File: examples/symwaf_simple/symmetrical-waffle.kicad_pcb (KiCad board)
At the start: 2 copper layers, 38 parts, among them J1 ICSP, J2 FTDI Programmer, J3 GPIO Header, SW1 SW_Push, SW2 SW_DIP_x01, U1 ATMEGA328-AU, U10 ws2812b, U11 ws2812b, U12 ws2812b, U13 ws2812b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

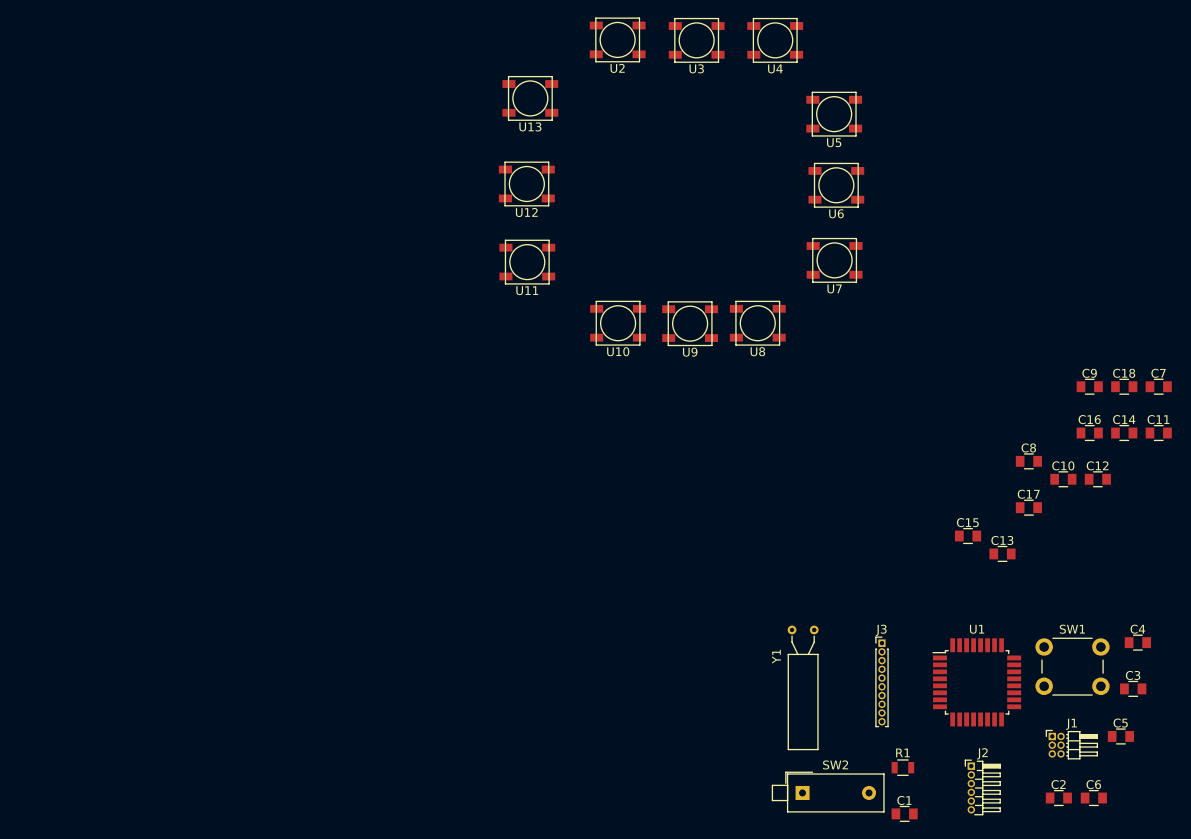
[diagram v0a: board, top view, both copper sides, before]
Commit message: Creating a simpler version of the example board
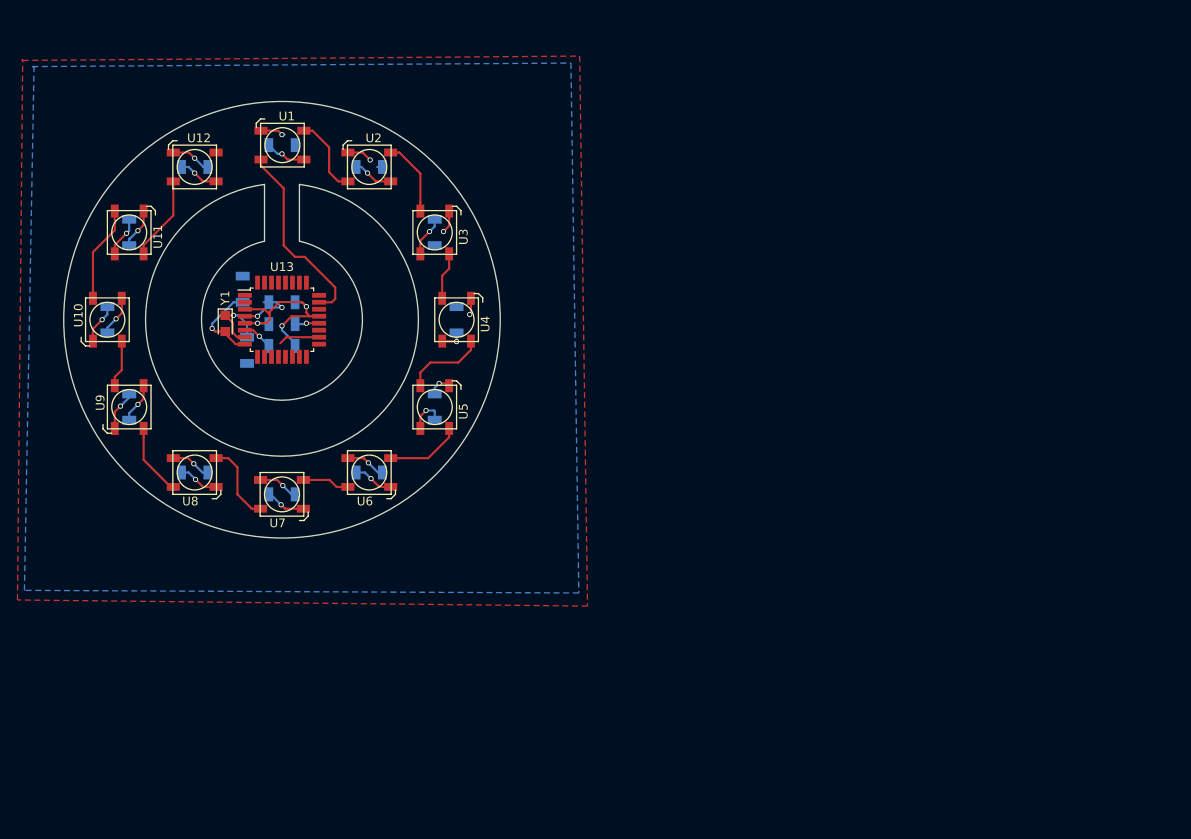
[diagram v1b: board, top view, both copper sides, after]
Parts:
- removed C18: C, Capacitors_SMD:C_0805
- removed J1: ICSP, Pin_Headers:Pin_Header_Angled_2x03_Pitch1.00mm
- removed J2: FTDI Programmer, Pin_Headers:Pin_Header_Angled_1x06_Pitch1.00mm
- removed J3: GPIO Header, Pin_Headers:Pin_Header_Straight_1x10_Pitch1.00mm
- removed R1: 10K, Resistors_SMD:R_0805
- removed SW1: SW_Push, Buttons_Switches_THT:SW_PUSH_6mm_h5mm
- removed SW2: SW_DIP_x01, Buttons_Switches_THT:SW_DIP_x1_W7.62mm_Piano
- C1, C2, C3: value 1nF -> C; footprint Capacitors_SMD:C_0805 -> Capacitors_SMD:C_1206; moved to B.Cu
- C10, C11, C12, C7, C8, C9: footprint Capacitors_SMD:C_0805 -> Capacitors_SMD:C_1206; moved to B.Cu
- C13, C14, C15: value C -> 1nF; footprint Capacitors_SMD:C_0805 -> Capacitors_SMD:C_1206; moved to B.Cu
- C16, C17: value C -> 22pF; footprint Capacitors_SMD:C_0805 -> Capacitors_SMD:C_1206; moved to B.Cu
- C4: value 100nF -> C; footprint Capacitors_SMD:C_0805 -> Capacitors_SMD:C_1206; moved to B.Cu
- C5, C6: value 22pF -> C; footprint Capacitors_SMD:C_0805 -> Capacitors_SMD:C_1206; moved to B.Cu
- U1: value ATMEGA328-AU -> ws2812b; footprint Housings_QFP:TQFP-32_7x7mm_Pitch0.8mm -> symwaf:ws2812b
- U13: value ws2812b -> ATMEGA328-AU; footprint symwaf:ws2812b -> Housings_QFP:TQFP-32_7x7mm_Pitch0.8mm
- Y1: footprint Crystals:Crystal_AT310_d3.0mm_l10.0mm_Horizontal -> Crystals:Crystal_SMD_2012-2pin_2.0x1.2mm_HandSoldering
- moved C11 120.1 mm to (70.0, 85.0), turned to 270 degrees
- moved C10 111.0 mm to (67.5, 95.0), turned to 90 degrees
- moved C9 110.0 mm to (70.0, 105.0), turned to 90 degrees
- moved C12 109.5 mm to (77.5, 77.5)
- moved C2 107.1 mm to (97.5, 77.5)
- moved C1 104.7 mm to (87.5, 75.0)
- moved C7 101.2 mm to (87.5, 115.0), turned to 180 degrees
- moved U1 100.6 mm to (87.5, 75.0), turned to 180 degrees
- moved C14 97.0 mm to (87.5, 98.0)
- moved C16 97.0 mm to (83.5, 98.5), turned to 90 degrees
- moved C3 95.6 mm to (105.0, 85.0), turned to 270 degrees
- moved C8 95.6 mm to (77.5, 112.5), turned to 180 degrees
- moved C17 93.5 mm to (83.0, 91.5), turned to 270 degrees
- moved C6 91.0 mm to (97.5, 112.5), turned to 180 degrees
- moved C13 87.4 mm to (87.5, 93.0)
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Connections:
- C15 pad 1: VCC -> Net-(C15-Pad1)
- C16 pad 1: VCC -> GND
- C16 pad 2: GND -> /XTAL1
- C17 pad 1: VCC -> GND
- C17 pad 2: GND -> /XTAL2
- C3 pad 1: Net-(C3-Pad1) -> VCC
- C4 pad 1: /DTR -> VCC
- C4 pad 2: /RST_CIRCUIT -> GND
- C5 pad 1: GND -> VCC
- C5 pad 2: /XTAL1 -> GND
- C6 pad 1: GND -> VCC
- C6 pad 2: /XTAL2 -> GND
- U1 pad 1: /GPIO_3 -> VCC
- U1 pad 2: /GPIO_4 -> Net-(U1-Pad2)
- U1 pad 4: VCC -> /LEDSignal
- U13 pad 1: VCC -> Net-(U13-Pad1)
- U13 pad 4: Net-(U12-Pad2) -> VCC
- U2 pad 4: /LEDSignal -> Net-(U1-Pad2)
- U6 pad 2: Net-(U6-Pad2) -> /LED Ring/ROW_2
- U7 pad 2: /LED Ring/ROW_2 -> Net-(U7-Pad2)
- U7 pad 4: Net-(U6-Pad2) -> /LED Ring/ROW_2
- U8 pad 4: /LED Ring/ROW_2 -> Net-(U7-Pad2)
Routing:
- net GND: track 0.00 -> 69.7 mm, vias 0 -> 15
- net VCC: track 0.00 -> 68.7 mm, vias 0 -> 15
- net /LEDSignal: track 0.00 -> 22.1 mm
- net Net-(U10-Pad2): track 0.00 -> 11.0 mm
- net Net-(U11-Pad2): track 0.00 -> 9.71 mm
- net /XTAL2: track 0.00 -> 9.71 mm, vias 0 -> 1
- net Net-(U4-Pad2): track 0.00 -> 9.38 mm
- net Net-(U7-Pad2): track 0.00 -> 9.32 mm
- net Net-(U1-Pad2): track 0.00 -> 9.12 mm
- net Net-(U5-Pad2): track 0.00 -> 8.69 mm
- net Net-(U2-Pad2): track 0.00 -> 8.69 mm
- net /XTAL1: track 0.00 -> 8.36 mm, vias 0 -> 1
- net Net-(U8-Pad2): track 0.00 -> 8.28 mm
- net Net-(U3-Pad2): track 0.00 -> 5.43 mm
- net Net-(U10-Pad4): track 0.00 -> 5.43 mm
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- added copper zone on B.Cu, net GND
- added copper zone on F.Cu, net VCC
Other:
- board outline added: 50 x 50 mm
